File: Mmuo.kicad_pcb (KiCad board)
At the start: 4 copper layers, 99.3 x 46.2 mm, 100 parts, among them IC1 A121-001-T&R, IC2 BQ24253RGER, IC3 ADPL40502AUJZ-1.8-R7, IC4 RAA2361052GNP#HC5, J1 USB_C_Receptacle_USB2.0_16P, J2 B2B-PH-K-S, J3 SW_Debug, Q1 BSS84, Q2 BSS138, Q3 MMBT3904, SW1 PTS815, U1 USBLC6-2SC6, U3 EKMB1309113K, U4 STM32WB55CGU6, Y1 24MHz, Y2 32MHz, Y3 32K768

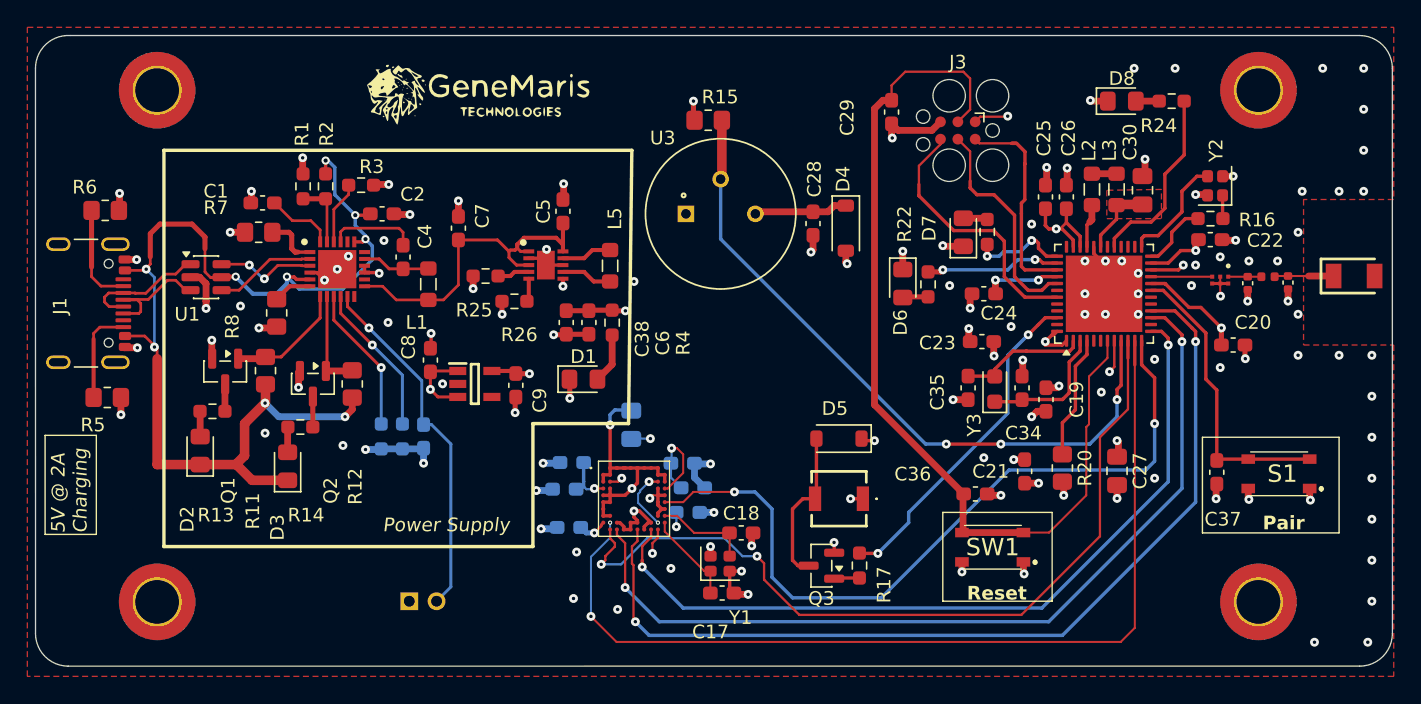
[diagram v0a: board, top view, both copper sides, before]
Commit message: V2.0: using a TOF sensor instead of a mmWave sensor
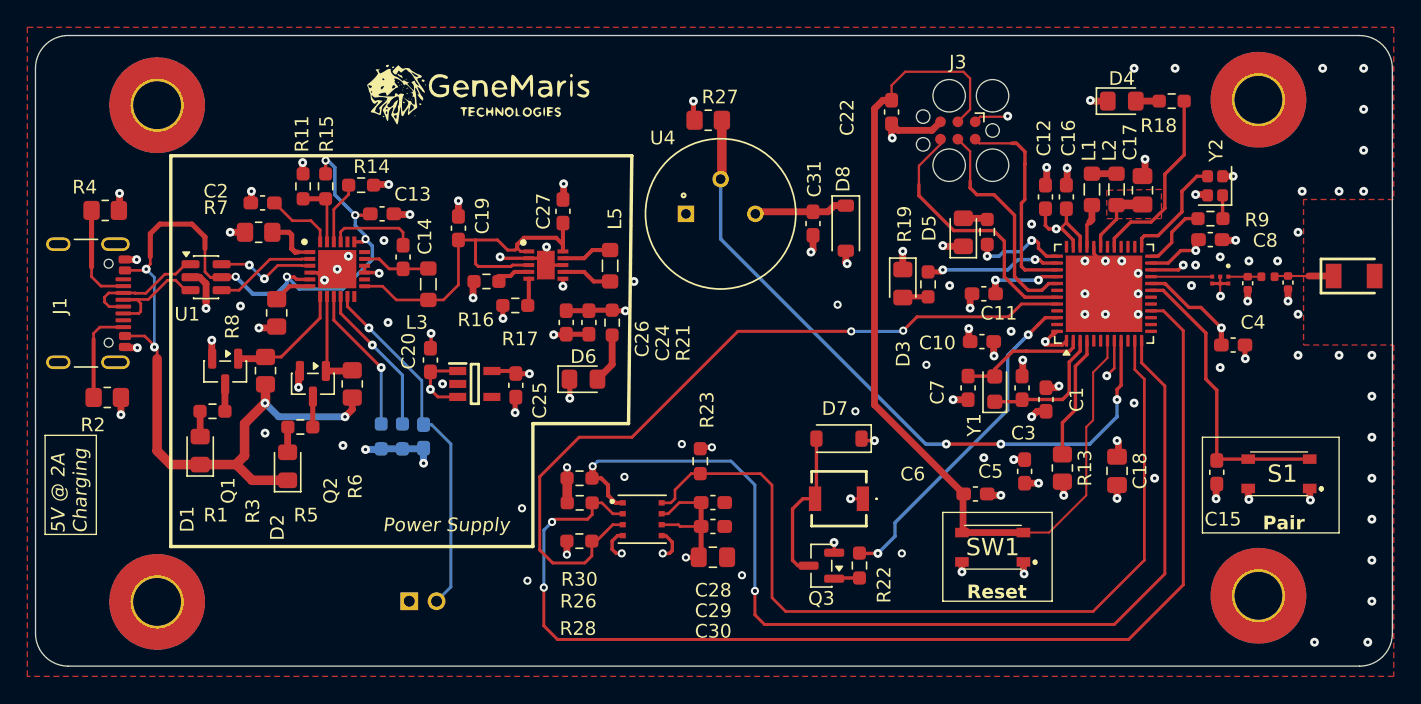
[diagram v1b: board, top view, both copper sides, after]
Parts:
- removed the C10 at (139.9, 113.0)
- removed the C11 at (148.1, 113.1)
- removed the C12 at (139.4, 115.0)
- removed the C13 at (148.8, 114.9)
- removed the C14 at (148.4, 116.7)
- removed the C15 at (144.3, 110.3)
- removed the C17 at (150.9, 122.6)
- removed the C18 at (152.3, 118.2)
- removed the C3 at (139.7, 117.8)
- removed the IC1 at (144.5, 115.7)
- removed the Y1 at (150.8, 120.4)
- added C28: 0u1, Capacitor_SMD:C_0603_1608Metric_Pad1.08x0.95mm_HandSolder, F.Cu at (150.3, 116.0)
- added C29: 0u1, Capacitor_SMD:C_0603_1608Metric_Pad1.08x0.95mm_HandSolder, F.Cu at (150.3, 117.7)
- added C30: 4u7, Capacitor_SMD:C_0805_2012Metric_Pad1.18x1.45mm_HandSolder, F.Cu at (150.3, 120.0)
- added R23: 10K, Resistor_SMD:R_0603_1608Metric_Pad0.98x0.95mm_HandSolder, F.Cu at (149.3, 112.9)
- added R26: 2k2, Resistor_SMD:R_0603_1608Metric_Pad0.98x0.95mm_HandSolder, F.Cu at (140.5, 116.0)
- added R28: 2k2, Resistor_SMD:R_0603_1608Metric_Pad0.98x0.95mm_HandSolder, F.Cu at (140.5, 118.8)
- added R30: 10K, Resistor_SMD:R_0603_1608Metric_Pad0.98x0.95mm_HandSolder, F.Cu at (140.5, 114.2)
- added U3: CH201-00ABR, CH201-00ABR:XDCR_CH201-00ABR, F.Cu at (145.1, 117.2)
- H1, H2, H3, H4: footprint MountingHole:MountingHole_3.2mm_M3_DIN965_Pad_TopBottom -> MountingHole:MountingHole_3.5mm_Pad_TopBottom
- moved H1 1.10 mm to (109.6, 86.9)
- moved H4 0.70 mm to (190.2, 86.5)
- moved H3 0.45 mm to (190.2, 122.8)
- moved R16 0.40 mm to (133.7, 99.8)
- moved R17 0.31 mm to (135.8, 101.5)
- renumbered AE2 to AE1, AE1 to AE2, C19 to C1, C23 to C10, C24 to C11, C25 to C12, C2 to C13, C4 to C14, C37 to C15, C26 to C16, C30 to C17, C27 to C18, C7 to C19, C1 to C2, C8 to C20, C32 to C21, C29 to C22, C33 to C23, C6 to C24, C9 to C25, C38 to C26, C5 to C27, C34 to C3, C28 to C31, C20 to C4, C21 to C5, C36 to C6, C35 to C7, C22 to C8, C16 to C9, D2 to D1, D3 to D2, D6 to D3, D8 to D4, D7 to D5, D1 to D6, D5 to D7, D4 to D8, IC2 to IC1, IC4 to IC2, L2 to L1, L3 to L2, L1 to L3, R13 to R1, R1 to R11, R9 to R12, R20 to R13, R3 to R14, R2 to R15, R25 to R16, R26 to R17, R24 to R18, R22 to R19, R5 to R2, R23 to R20, R4 to R21, R17 to R22, R15 to R27, R11 to R3, R6 to R4, R14 to R5, R12 to R6, R16 to R9, U4 to U2, U3 to U4, Y3 to Y1
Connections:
- U2 pad 10: /SPI_CLK -> unconnected-(U2-PA1-Pad10)
- U2 pad 11: /SPI_SS -> /TOF_~{RST}
- U2 pad 12: /SPI_EN -> /TOF_INT
- U2 pad 13: /SPI_INT -> unconnected-(U2-PA4-Pad13)
- U2 pad 15: /SPI_MISO -> unconnected-(U2-PA6-Pad15)
- U2 pad 16: /SPI_MOSI -> /TOF_SCL
- U2 pad 44: unconnected-(U4-PB4-Pad44) -> /TOF_SDA
- U2 pad 5: /Temp_SCL -> unconnected-(U2-PB8-Pad5)
- U2 pad 6: /Temp_SDA -> unconnected-(U2-PB9-Pad6)
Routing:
- net /TOF_SCL: track 0.00 -> 84.9 mm, vias 0 -> 2
- net /TOF_INT: track 0.00 -> 76.2 mm, vias 0 -> 2
- net /SPI_SS: track 69.5 -> 0.00 mm, vias 2 -> 0
- net /SPI_MOSI: track 68.8 -> 0.00 mm, vias 2 -> 0
- net /SPI_MISO: track 64.4 -> 0.00 mm, vias 2 -> 0
- net /TOF_~{RST}: track 0.00 -> 63.5 mm
- net /SPI_CLK: track 61.0 -> 0.00 mm, vias 2 -> 0
- net /SPI_INT: track 58.6 -> 0.00 mm, vias 2 -> 0
- net /TOF_SDA: track 0.00 -> 56.7 mm, vias 0 -> 2
- net /SPI_EN: track 55.6 -> 0.00 mm, vias 2 -> 0
- net GND: track 123.8 -> 89.4 mm, vias 129 -> 123
- net Net-(IC1-XOUT): track 6.96 -> 0.00 mm
- net Net-(IC1-XIN): track 6.81 -> 0.00 mm
- net +1V8: track 22.4 -> 18.5 mm, vias 8 -> 5
- net +3V3: track 61.8 -> 58.0 mm, vias 19 -> 17
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
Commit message: 25_12_22_10
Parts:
- moved D8 7.30 mm to (157.1, 89.2), turned to 90 degrees
- moved C31 2.27 mm to (158.3, 97.7), turned to 0 degrees
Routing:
- net GND: track 89.4 -> 84.0 mm, vias 123 -> 120
- net +3V3: track 58.0 -> 60.8 mm
- net /SMPSFB: track 5.45 -> 3.60 mm
